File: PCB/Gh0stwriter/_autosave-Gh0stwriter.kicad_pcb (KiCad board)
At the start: 2 copper layers, 81.3 x 68.6 mm, 19 parts, among them J1 Conn_01x06, J2 Conn_01x02, J3 Conn_01x06, J4 Conn_01x02, J5 Conn_01x06, J6 Conn_01x06, J7 Conn_01x02, Q1 Q_NPN_Darlington_ECB

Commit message: Most of pcb finished
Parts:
- added R1: R, Resistor_THT:R_Axial_DIN0207_L6.3mm_D2.5mm_P10.16mm_Horizontal, F.Cu at (203.2, 55.9)
- C1, C2: footprint Capacitor_THT:CP_Radial_D8.0mm_P2.50mm -> Capacitor_THT:CP_Radial_D6.3mm_P2.50mm
- D1: footprint Diode_THT:D_DO-41_SOD81_P10.16mm_Horizontal -> Diode_THT:D_DO-35_SOD27_P2.54mm_Vertical_AnodeUp
- moved D1 131.8 mm to (203.2, 43.2), turned to 180 degrees
- moved J4 121.9 mm to (203.2, 48.3), turned to 180 degrees
- moved J2 104.1 mm to (198.1, 62.2), turned to 90 degrees
- moved Q1 98.0 mm to (198.1, 53.3)
- moved SerialPort1 96.7 mm to (193.0, 63.5), turned to 270 degrees
- moved C4 73.9 mm to (125.7, 53.3)
- moved C2 71.7 mm to (128.3, 49.5), turned to 90 degrees
- moved C1 62.6 mm to (154.9, 63.5)
- moved C3 59.4 mm to (154.9, 58.4)
- moved J1 40.2 mm to (147.3, 53.3)
- moved J7 18.0 mm to (203.2, 38.1)
- moved A2 15.2 mm to (147.3, 30.5)
- moved J3 15.2 mm to (147.2, 25.4)
- moved A3 12.7 mm to (170.2, 30.5)
- moved J5 12.7 mm to (170.1, 25.4)
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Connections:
- BP?1 pad 1: ICReset -> Hammer
- BP?1 pad 2: Net-(BP?1-Pad2) -> ICReset
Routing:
- net GND: track 0.00 -> 216.7 mm, vias 0 -> 5
- net +3V3: track 0.00 -> 165.1 mm, vias 0 -> 4
- net Vdrive: track 0.00 -> 134.6 mm, vias 0 -> 2
- net Net-(D1-Pad2): track 0.00 -> 10.2 mm
- net PA9: track 0.00 -> 7.62 mm
- net PA10: track 0.00 -> 7.62 mm
- net Net-(A4-Pad6): track 0.00 -> 5.16 mm
- net Net-(A1-Pad6): track 0.00 -> 5.16 mm
- net Net-(A4-Pad5): track 0.00 -> 5.15 mm
- net Net-(A1-Pad5): track 0.00 -> 5.15 mm
- net Net-(A4-Pad4): track 0.00 -> 5.13 mm
- net Net-(A2-Pad6): track 0.00 -> 5.13 mm
- net Net-(A1-Pad4): track 0.00 -> 5.13 mm
- net Net-(A3-Pad6): track 0.00 -> 5.11 mm
- net Net-(A2-Pad5): track 0.00 -> 5.11 mm
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
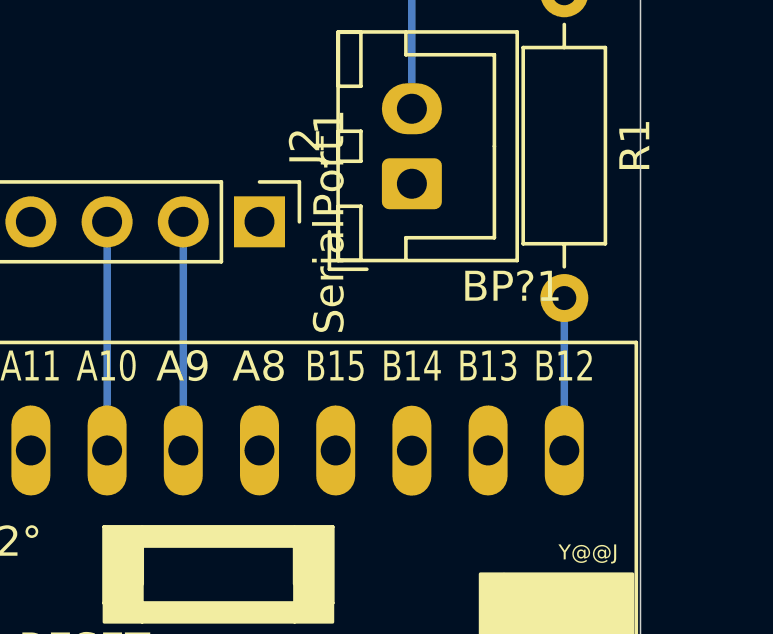
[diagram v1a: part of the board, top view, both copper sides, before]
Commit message: Fixed clipping of parts
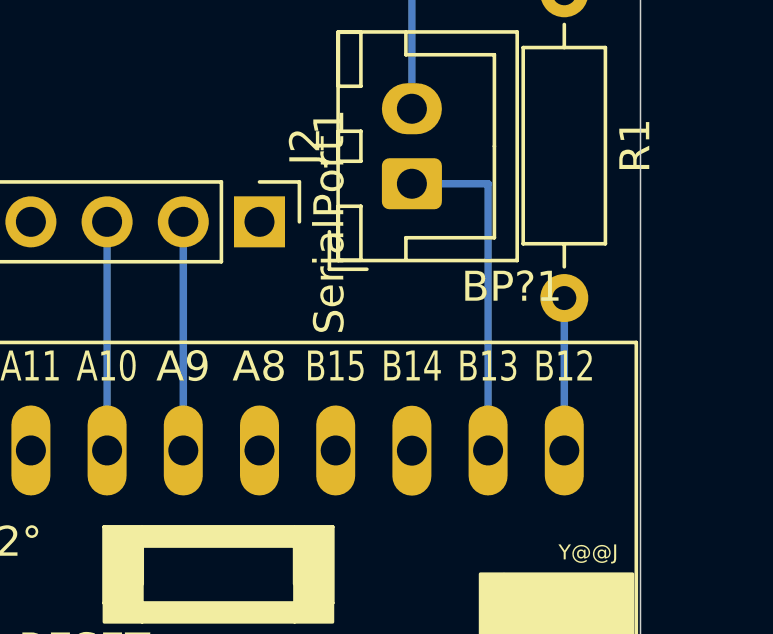
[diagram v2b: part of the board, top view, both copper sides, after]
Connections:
- BP?1 pad 2: ICReset -> Endstop
- J2 pad 1: Net-(J2-Pad1) -> Endstop
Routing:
- net Endstop: track 0.00 -> 11.4 mm
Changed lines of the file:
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@@
     (thickness 1.6)
     (drawings 4)
-    (tracks 124)
+    (tracks 126)
     (zones 0)
     (modules 20)
@@
   (net 82 PA9)
   (net 83 "Net-(D1-Pad2)")
-  (net 84 "Net-(J2-Pad1)")
-  (net 85 "Net-(Q1-Pad3)")
-  (net 86 "Net-(SerialPort1-Pad5)")
-  (net 87 "Net-(SerialPort1-Pad4)")
-  (net 88 "Net-(SerialPort1-Pad1)")
-  (net 89 "Net-(J1-Pad2)")
-  (net 90 "Net-(J1-Pad1)")
-  (net 91 "Net-(J3-Pad1)")
-  (net 92 "Net-(J3-Pad2)")
-  (net 93 "Net-(J5-Pad2)")
-  (net 94 "Net-(J5-Pad1)")
-  (net 95 "Net-(J6-Pad1)")
-  (net 96 "Net-(J6-Pad2)")
-  (net 97 Hammer)
+  (net 84 "Net-(Q1-Pad3)")
+  (net 85 "Net-(SerialPort1-Pad5)")
+  (net 86 "Net-(SerialPort1-Pad4)")
+  (net 87 "Net-(SerialPort1-Pad1)")
+  (net 88 "Net-(J1-Pad2)")
+  (net 89 "Net-(J1-Pad1)")
+  (net 90 "Net-(J3-Pad1)")
+  (net 91 "Net-(J3-Pad2)")
+  (net 92 "Net-(J5-Pad2)")
+  (net 93 "Net-(J5-Pad1)")
+  (net 94 "Net-(J6-Pad1)")
+  (net 95 "Net-(J6-Pad2)")
+  (net 96 Hammer)
+  (net 97 Endstop)
   (net_class Default "This is the default net class."
     (clearance 0.2)
@@
     (uvia_drill 0.1)
     (add_net +3V3)
+    (add_net Endstop)
     (add_net GND)
     (add_net Hammer)
@@
     (add_net "Net-(J1-Pad1)")
     (add_net "Net-(J1-Pad2)")
-    (add_net "Net-(J2-Pad1)")
     (add_net "Net-(J3-Pad1)")
     (add_net "Net-(J3-Pad2)")
@@
     )
     (pad 3 thru_hole oval (at 5.08 0) (size 1.8 1.8) (drill 1) (layers *.Cu *.Mask)
-      (net 85 "Net-(Q1-Pad3)"))
+      (net 84 "Net-(Q1-Pad3)"))
     (pad 2 thru_hole oval (at 2.54 0) (size 1.8 1.8) (drill 1) (layers *.Cu *.Mask)
       (net 83 "Net-(D1-Pad2)"))
@@
       (net 45 GND))
     (pad 1 thru_hole roundrect (at 0 0 90) (size 1.7 2) (drill 1) (layers *.Cu *.Mask) (roundrect_rratio 0.147059)
-      (net 84 "Net-(J2-Pad1)"))
+      (net 97 Endstop))
     (model ${KISYS3DMOD}/Connector_JST.3dshapes/JST_XH_B2B-XH-A_1x02_P2.50mm_Vertical.wrl
       (at (xyz 0 0 0))
@@
       (net 43 "Net-(BP?1-Pad38)"))
     (pad 2 thru_hole oval (at 2.54 0 180) (size 1.3 3) (drill 1) (layers *.Cu *.Mask)
-      (net 46 ICReset))
+      (net 97 Endstop))
     (pad 39 thru_hole oval (at 2.54 -15.24762 180) (size 1.3 3) (drill 1) (layers *.Cu *.Mask)
       (net 45 GND))
     (pad 1 thru_hole oval (at 0 0 180) (size 1.3 3) (drill 1) (layers *.Cu *.Mask)
-      (net 97 Hammer))
+      (net 96 Hammer))
     (pad 40 thru_hole oval (at 0 -15.24762 180) (size 1.3 3) (drill 1) (layers *.Cu *.Mask)
       (net 45 GND))
@@
       (net 3 "Net-(A1-Pad3)"))
     (pad 2 thru_hole oval (at 2.5 0 180) (size 1.7 1.95) (drill 0.95) (layers *.Cu *.Mask)
-      (net 89 "Net-(J1-Pad2)"))
+      (net 88 "Net-(J1-Pad2)"))
     (pad 1 thru_hole roundrect (at 0 0 180) (size 1.7 1.95) (drill 0.95) (layers *.Cu *.Mask) (roundrect_rratio 0.147059)
-      (net 90 "Net-(J1-Pad1)"))
+      (net 89 "Net-(J1-Pad1)"))
     (model ${KISYS3DMOD}/Connector_JST.3dshapes/JST_XH_B6B-XH-A_1x06_P2.50mm_Vertical.wrl
       (at (xyz 0 0 0))
@@
     )
     (pad 1 thru_hole roundrect (at 0 0 180) (size 1.7 1.95) (drill 0.95) (layers *.Cu *.Mask) (roundrect_rratio 0.147059)
-      (net 91 "Net-(J3-Pad1)"))
+      (net 90 "Net-(J3-Pad1)"))
     (pad 2 thru_hole oval (at 2.5 0 180) (size 1.7 1.95) (drill 0.95) (layers *.Cu *.Mask)
-      (net 92 "Net-(J3-Pad2)"))
+      (net 91 "Net-(J3-Pad2)"))
     (pad 3 thru_hole oval (at 5 0 180) (size 1.7 1.95) (drill 0.95) (layers *.Cu *.Mask)
       (net 56 "Net-(A2-Pad3)"))
@@
       (net 61 "Net-(A3-Pad3)"))
     (pad 2 thru_hole oval (at 2.5 0 180) (size 1.7 1.95) (drill 0.95) (layers *.Cu *.Mask)
-      (net 93 "Net-(J5-Pad2)"))
+      (net 92 "Net-(J5-Pad2)"))
     (pad 1 thru_hole roundrect (at 0 0 180) (size 1.7 1.95) (drill 0.95) (layers *.Cu *.Mask) (roundrect_rratio 0.147059)
-      (net 94 "Net-(J5-Pad1)"))
+      (net 93 "Net-(J5-Pad1)"))
     (model ${KISYS3DMOD}/Connector_JST.3dshapes/JST_XH_B6B-XH-A_1x06_P2.50mm_Vertical.wrl
       (at (xyz 0 0 0))
@@
     )
     (pad 1 thru_hole roundrect (at 0 0 180) (size 1.7 1.95) (drill 0.95) (layers *.Cu *.Mask) (roundrect_rratio 0.147059)
-      (net 95 "Net-(J6-Pad1)"))
+      (net 94 "Net-(J6-Pad1)"))
     (pad 2 thru_hole oval (at 2.5 0 180) (size 1.7 1.95) (drill 0.95) (layers *.Cu *.Mask)
-      (net 96 "Net-(J6-Pad2)"))
+      (net 95 "Net-(J6-Pad2)"))
     (pad 3 thru_hole oval (at 5 0 180) (size 1.7 1.95) (drill 0.95) (layers *.Cu *.Mask)
       (net 78 "Net-(A4-Pad3)"))
@@
     )
     (pad 1 thru_hole rect (at 0 0 270) (size 1.7 1.7) (drill 1) (layers *.Cu *.Mask)
-      (net 88 "Net-(SerialPort1-Pad1)"))
+      (net 87 "Net-(SerialPort1-Pad1)"))
     (pad 2 thru_hole oval (at 0 2.54 270) (size 1.7 1.7) (drill 1) (layers *.Cu *.Mask)
       (net 82 PA9))
@@
       (net 81 PA10))
     (pad 4 thru_hole oval (at 0 7.62 270) (size 1.7 1.7) (drill 1) (layers *.Cu *.Mask)
-      (net 87 "Net-(SerialPort1-Pad4)"))
+      (net 86 "Net-(SerialPort1-Pad4)"))
     (pad 5 thru_hole oval (at 0 10.16 270) (size 1.7 1.7) (drill 1) (layers *.Cu *.Mask)
-      (net 86 "Net-(SerialPort1-Pad5)"))
+      (net 85 "Net-(SerialPort1-Pad5)"))
     (pad 6 thru_hole oval (at 0 12.7 270) (size 1.7 1.7) (drill 1) (layers *.Cu *.Mask)
       (net 45 GND))
@@
     )
     (pad 1 thru_hole circle (at 0 0 270) (size 1.6 1.6) (drill 0.8) (layers *.Cu *.Mask)
-      (net 85 "Net-(Q1-Pad3)"))
+      (net 84 "Net-(Q1-Pad3)"))
     (pad 2 thru_hole oval (at 10.16 0 270) (size 1.6 1.6) (drill 0.8) (layers *.Cu *.Mask)
-      (net 97 Hammer))
+      (net 96 Hammer))
     (model ${KISYS3DMOD}/Resistor_THT.3dshapes/R_Axial_DIN0207_L6.3mm_D2.5mm_P10.16mm_Horizontal.wrl
       (at (xyz 0 0 0))
@@
   (segment (start 200.66 48.3) (end 200.7 48.26) (width 0.25) (layer B.Cu) (net 83))
   (segment (start 200.66 53.34) (end 200.66 48.3) (width 0.25) (layer B.Cu) (net 83))
-  (segment (start 203.2 53.34) (end 203.2 55.88) (width 0.25) (layer B.Cu) (net 85))
-  (segment (start 203.2 66.04) (end 203.2 71.12) (width 0.25) (layer B.Cu) (net 97))
+  (segment (start 203.2 53.34) (end 203.2 55.88) (width 0.25) (layer B.Cu) (net 84))
+  (segment (start 203.2 66.04) (end 203.2 71.12) (width 0.25) (layer B.Cu) (net 96))
+  (segment (start 198.12 62.23) (end 200.66 62.23) (width 0.25) (layer B.Cu) (net 97))
+  (segment (start 200.66 62.23) (end 200.66 71.12) (width 0.25) (layer B.Cu) (net 97))
 )

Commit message: Finished first Version of the pcb
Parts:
- moved SerialPort1 2.54 mm to (193.0, 66.0), turned to 180 degrees
- moved J2 1.27 mm to (198.1, 63.5)
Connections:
- net Net-(A1-Pad15) renamed A1STP
- net Net-(A1-Pad16) renamed A1DIR
- A2 pad 15: Net-(A2-Pad15) -> A2STP
- A2 pad 16: Net-(A2-Pad16) -> A2DIR
- A3 pad 13: ICReset -> Net-(A3-Pad13)
- A3 pad 15: Net-(A3-Pad15) -> A3STP
- A3 pad 16: Net-(A3-Pad16) -> A3DIR
- A4 pad 15: Net-(A4-Pad15) -> A4STP
- A4 pad 16: Net-(A4-Pad16) -> A4DIR
- BP?1 pad 10: Net-(BP?1-Pad10) -> A4DIR
- BP?1 pad 11: Net-(BP?1-Pad11) -> A4STP
- BP?1 pad 12: Net-(BP?1-Pad12) -> ICReset
- BP?1 pad 13: Net-(BP?1-Pad13) -> A3DIR
- BP?1 pad 14: Net-(BP?1-Pad14) -> A3STP
- BP?1 pad 15: Net-(BP?1-Pad15) -> A2DIR
- BP?1 pad 16: Net-(BP?1-Pad16) -> A2STP
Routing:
- net ICReset: track 0.00 -> 91.4 mm
- net A4STP: track 0.00 -> 40.6 mm
- net A4DIR: track 0.00 -> 40.6 mm
- net +3V3: track 165.1 -> 129.5 mm
- net PA10: track 7.62 -> 15.2 mm
- net PA9: track 7.62 -> 10.2 mm
- net GND: track 216.7 -> 215.2 mm, vias 5 -> 4
- net Endstop: track 11.4 -> 10.2 mm
